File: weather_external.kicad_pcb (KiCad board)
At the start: 2 copper layers, 28.2 x 43.4 mm, 23 parts, among them J1 Conn_01x02_Male, J2 USB_B_Mini, J3 Conn_01x02_Male, J8 FTDI, SW1 SW_Push, U1 TP4056, U2 MCP1700T-3302E_TT

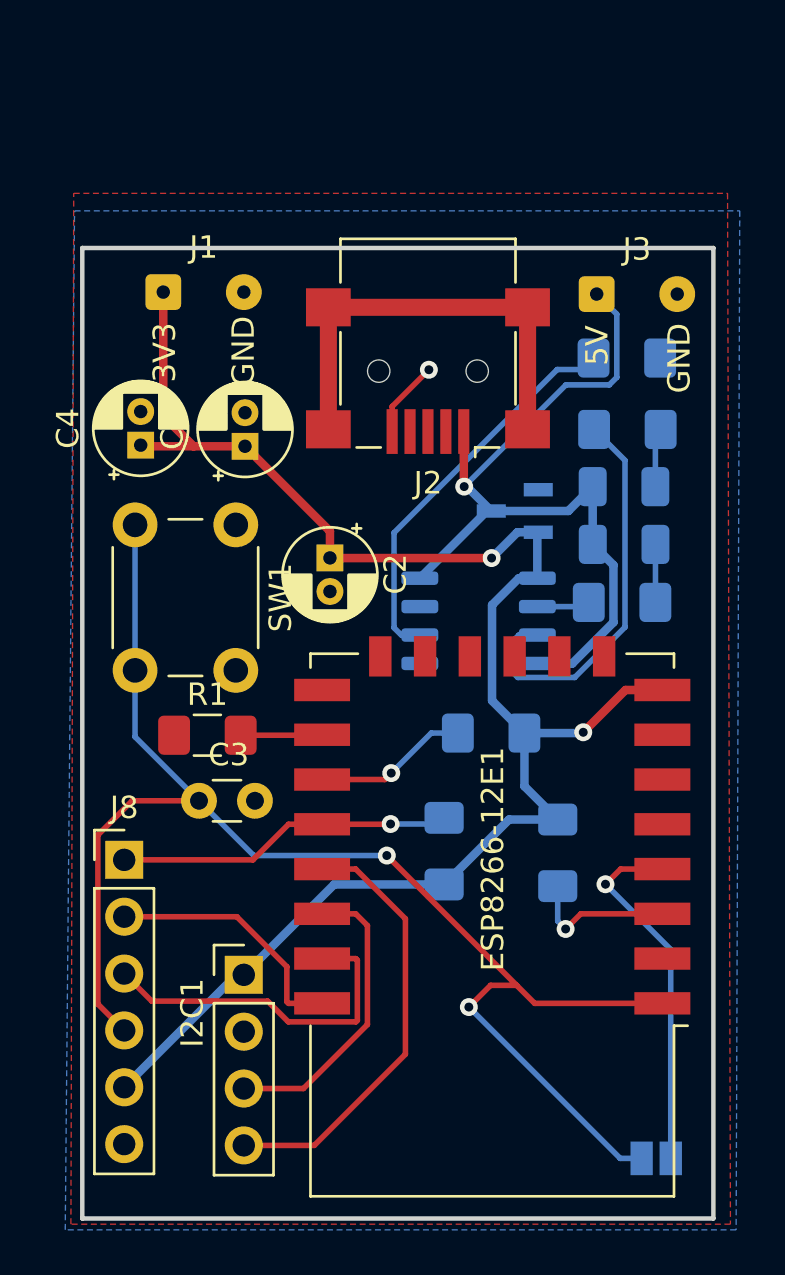
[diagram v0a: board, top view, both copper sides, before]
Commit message: Fixing some labels
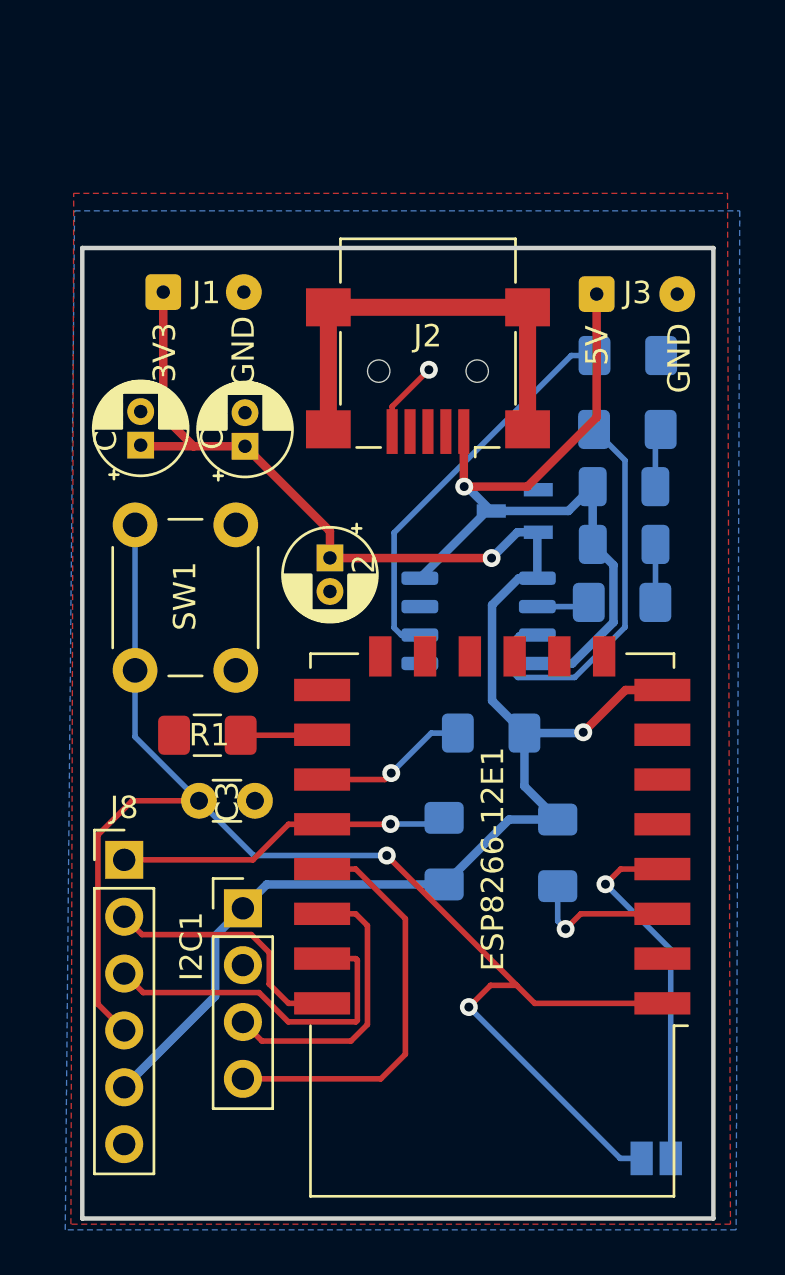
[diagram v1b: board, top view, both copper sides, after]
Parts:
- moved I2C1 2.97 mm to (3.11, 83.7)
- moved R7 0.12 mm to (20.3, 59.0)
- renumbered U1 to TP4056
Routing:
- net +3V3: track 75.2 -> 76.7 mm
- net SDA: track 19.6 -> 18.4 mm
- net Net-(R7-Pad1): track 18.1 -> 18.9 mm

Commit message: - Using MCP73831 to manage battery charging
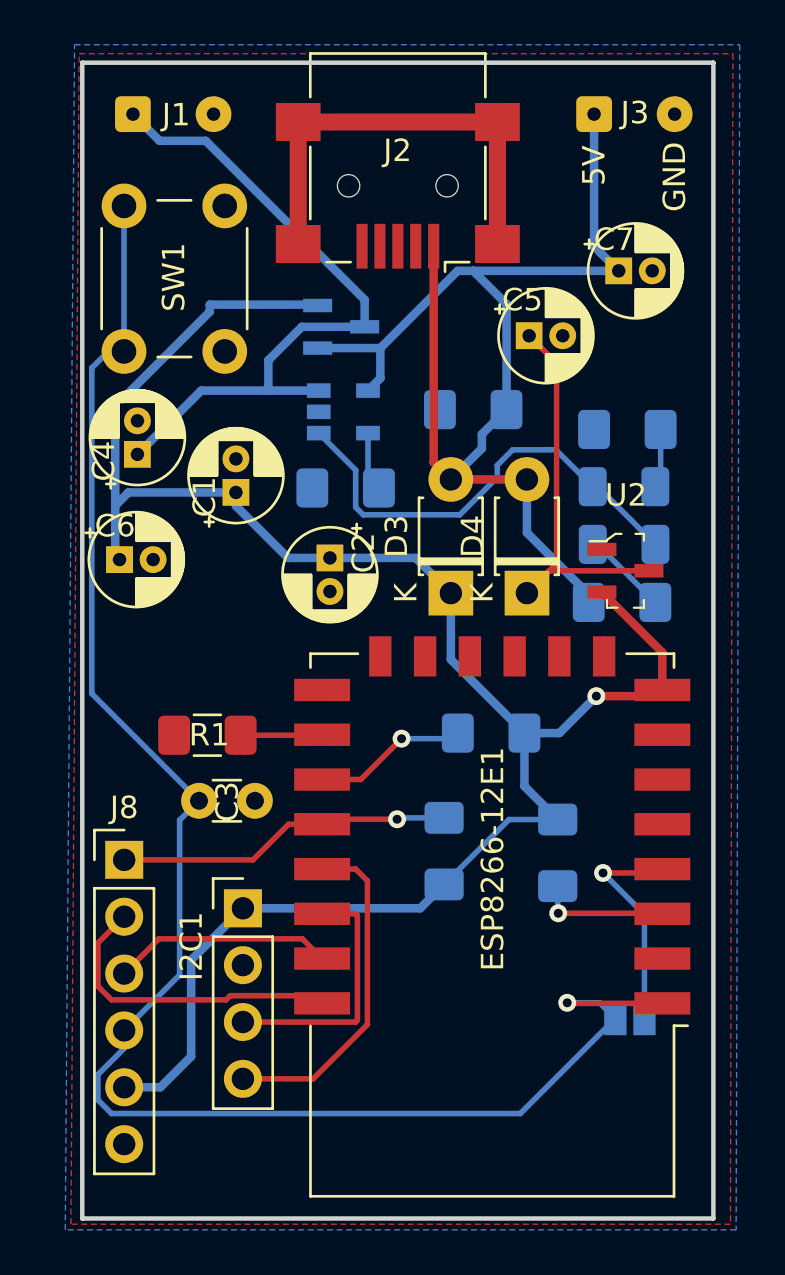
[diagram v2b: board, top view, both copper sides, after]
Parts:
- removed TP4056: TP4056, Package_SO:SOP-8_3.9x4.9mm_P1.27mm
- added C5: 10nF, Capacitor_THT:CP_Radial_D4.0mm_P1.50mm, F.Cu at (15.9, 58.1)
- added C6: 10nF, Capacitor_THT:CP_Radial_D4.0mm_P1.50mm, F.Cu at (-2.40, 68.1)
- added C7: CP, Capacitor_THT:CP_Radial_D4.0mm_P1.50mm, F.Cu at (19.9, 55.2)
- added D3: 1N4148, Diode_THT:D_T-1_P5.08mm_Horizontal, F.Cu at (12.4, 69.6)
- added D4: 1N4148, Diode_THT:D_T-1_P5.08mm_Horizontal, F.Cu at (15.8, 69.6)
- added Q1: DMG2305UX-13, digikey-footprints:SOT-23-3, B.Cu at (7.50, 57.7)
- added R8: 100k, Resistor_SMD:R_1206_3216Metric_Pad1.42x1.75mm_HandSolder, B.Cu at (13.4, 61.4)
- added U1: MCP73831-2-OT, Package_TO_SOT_SMD:SOT-23-5, B.Cu at (7.60, 61.5)
- D1: value LED -> GREEN
- D2: value LED -> RED
- R5, R6: value 1k -> 220
- R7: value 1k2 -> 2k
- U2: moved to F.Cu
- moved SW1 14.3 mm to (2.30, 52.3)
- moved R7 13.9 mm to (7.70, 64.9)
- moved J2 8.39 mm to (10.0, 51.4)
- moved J1 8.06 mm to (-1.80, 48.2)
- moved J3 8.04 mm to (18.8, 48.2)
- moved JP1 6.36 mm to (20.4, 88.6)
- moved U2 5.62 mm to (20.2, 68.6), turned to 0 degrees
- moved C1 2.10 mm to (2.80, 65.1)
- moved C4 0.44 mm to (-1.60, 63.4)
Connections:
- C4 pad 1: +3V3 -> VBAT
- D1 pad 2: VCC -> Net-(D1-Pad2)
- D2 pad 1: Net-(D2-Pad1) -> Net-(D1-Pad2)
- D2 pad 2: VCC -> Net-(D2-Pad2)
- J1 pad 1: +3V3 -> VBAT
- R5 pad 2: Net-(R5-Pad2) -> GND
- R6 pad 1: Net-(D2-Pad1) -> Net-(D2-Pad2)
- R6 pad 2: Net-(R6-Pad2) -> VCC
- R7 pad 1: Net-(R7-Pad1) -> GND
- R7 pad 2: GND -> Net-(R7-Pad2)
- U2 pad 3: VCC -> Net-(C5-Pad1)
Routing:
- net VBAT: track 0.00 -> 30.5 mm
- net Net-(D1-Pad2): track 0.00 -> 20.8 mm
- net VCC: track 36.9 -> 56.2 mm, vias 1 -> 0
- net Net-(R7-Pad1): track 18.9 -> 0.00 mm
- net Net-(C5-Pad1): track 0.00 -> 18.4 mm
- net Net-(R5-Pad2): track 18.1 -> 0.00 mm
- net RST: track 65.4 -> 76.9 mm, vias 2 -> 1
- net +3V3: track 76.7 -> 87.1 mm, vias 2 -> 1
- net GPIO16: track 16.3 -> 9.99 mm
- net RX: track 15.6 -> 9.85 mm
- net Net-(D2-Pad2): track 0.00 -> 3.87 mm
- net GND: track 3.76 -> 0.00 mm, vias 1 -> 0
- net SDA: track 18.4 -> 15.2 mm
- net TX: track 11.3 -> 14.1 mm
- net Net-(R7-Pad2): track 0.00 -> 2.65 mm
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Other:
- board size 28.2 x 43.4 mm -> 28.2 x 51.6 mm

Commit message: V1.4 - adding jumper to reset configurations(wifi and custom)
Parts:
- added J4: Conn_01x02_Male, Connector_PinHeader_2.54mm:PinHeader_1x02_P2.54mm_Vertical, F.Cu at (2.66, 70.0)
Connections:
- ESP8266-12E1 pad 7: (no net) -> GPIO13
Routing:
- net GPIO13: track 0.00 -> 21.6 mm, vias 0 -> 1
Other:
- board text added: "FACT"
- board text added: "Weather External v1.4"
- board text removed: "Weather External v1.3"

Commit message: Fixing FTDI labels
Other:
- board text added: "G"
- board text added: "V"

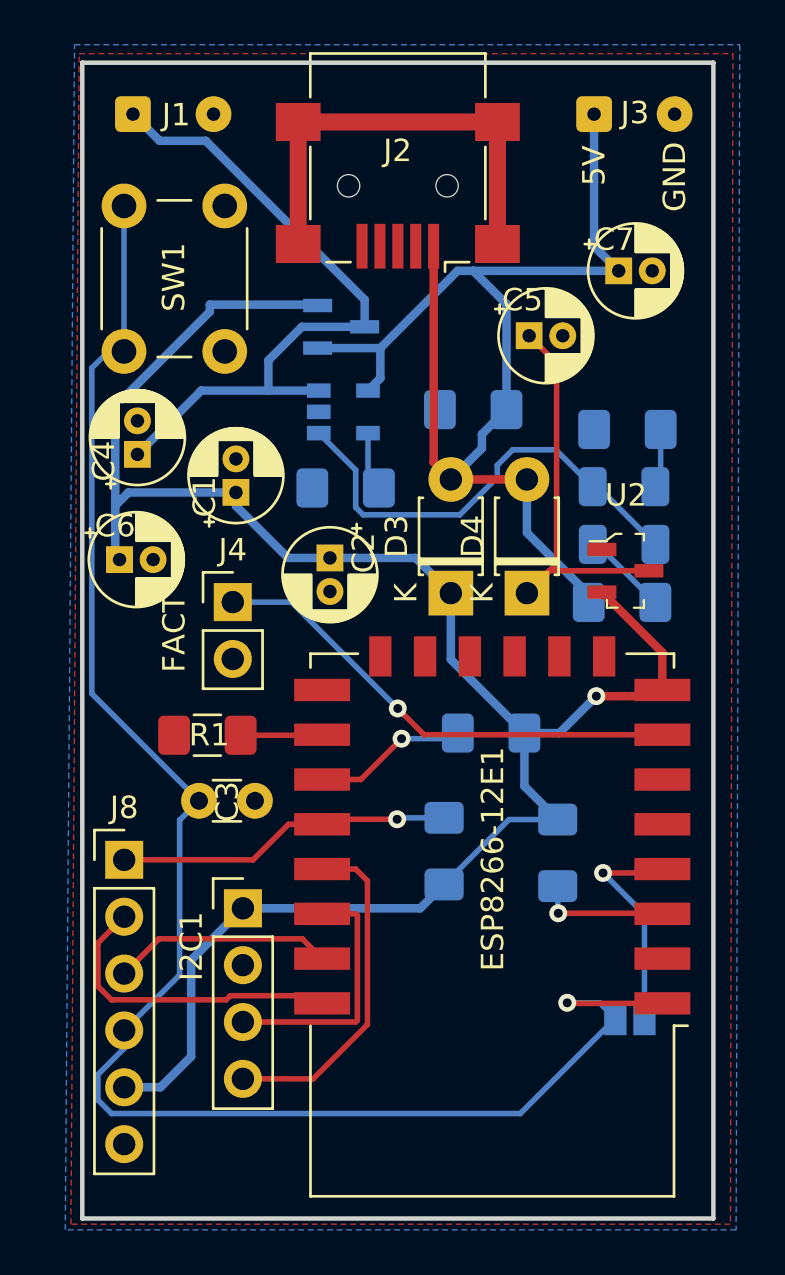
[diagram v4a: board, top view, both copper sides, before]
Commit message: - Moving BME280 farther from the ESP8266 Antenna - keeping the version
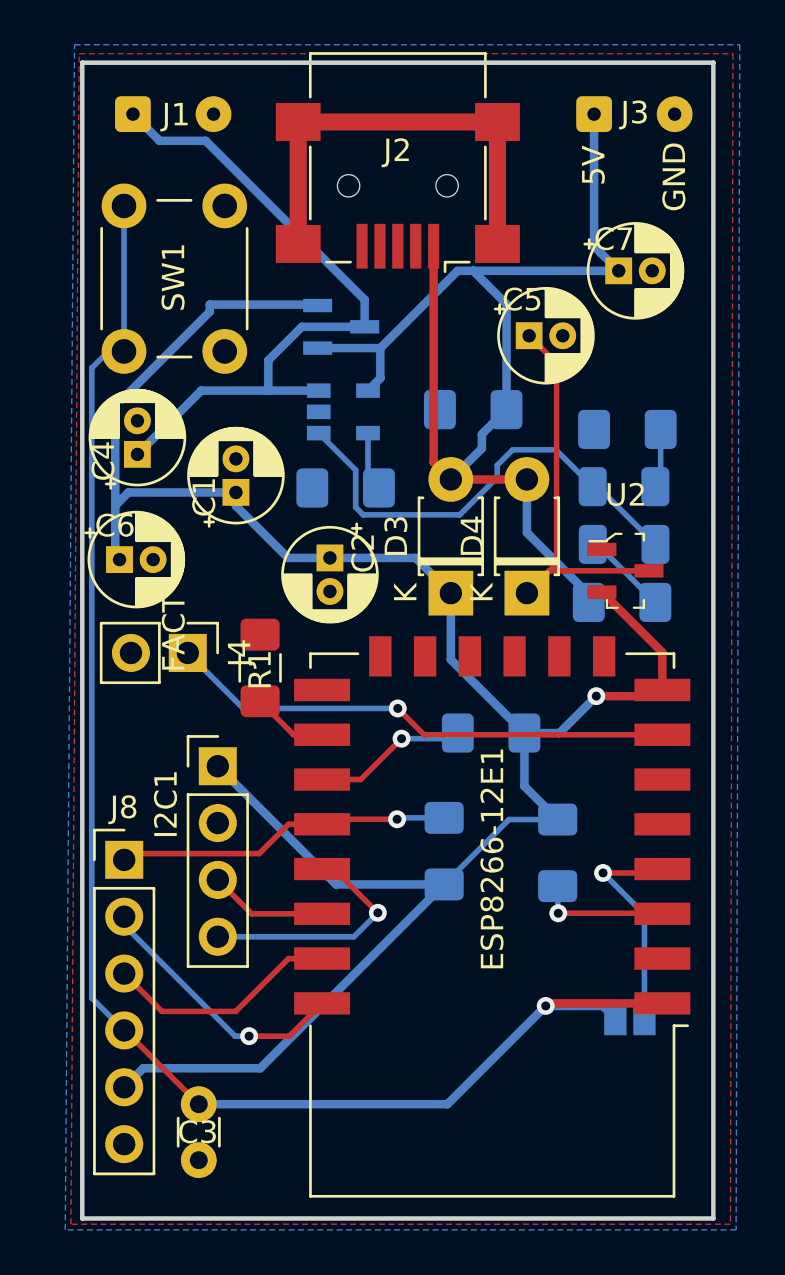
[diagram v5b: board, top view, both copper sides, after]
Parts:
- moved C3 16.3 mm to (1.14, 94.9), turned to 90 degrees
- moved I2C1 6.45 mm to (1.99, 77.3)
- moved R1 3.82 mm to (3.88, 72.9), turned to 270 degrees
- moved J4 3.03 mm to (0.65, 72.3), turned to 270 degrees
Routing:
- net +3V3: track 87.1 -> 96.9 mm
- net RST: track 76.9 -> 69.3 mm
- net SCL: track 11.4 -> 5.29 mm
- net SDA: track 15.2 -> 10.9 mm, vias 0 -> 1
- net TX: track 14.1 -> 12.4 mm, vias 0 -> 1
- net GPIO13: track 21.6 -> 22.7 mm
- net RX: track 9.85 -> 10.5 mm
